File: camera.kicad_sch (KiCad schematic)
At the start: 12 parts, among them J2 FPC-05F-22PH20, Q1 BSS138PW,115, Q2 BSS138PW,115, U1 AM6254ATCGHAALW

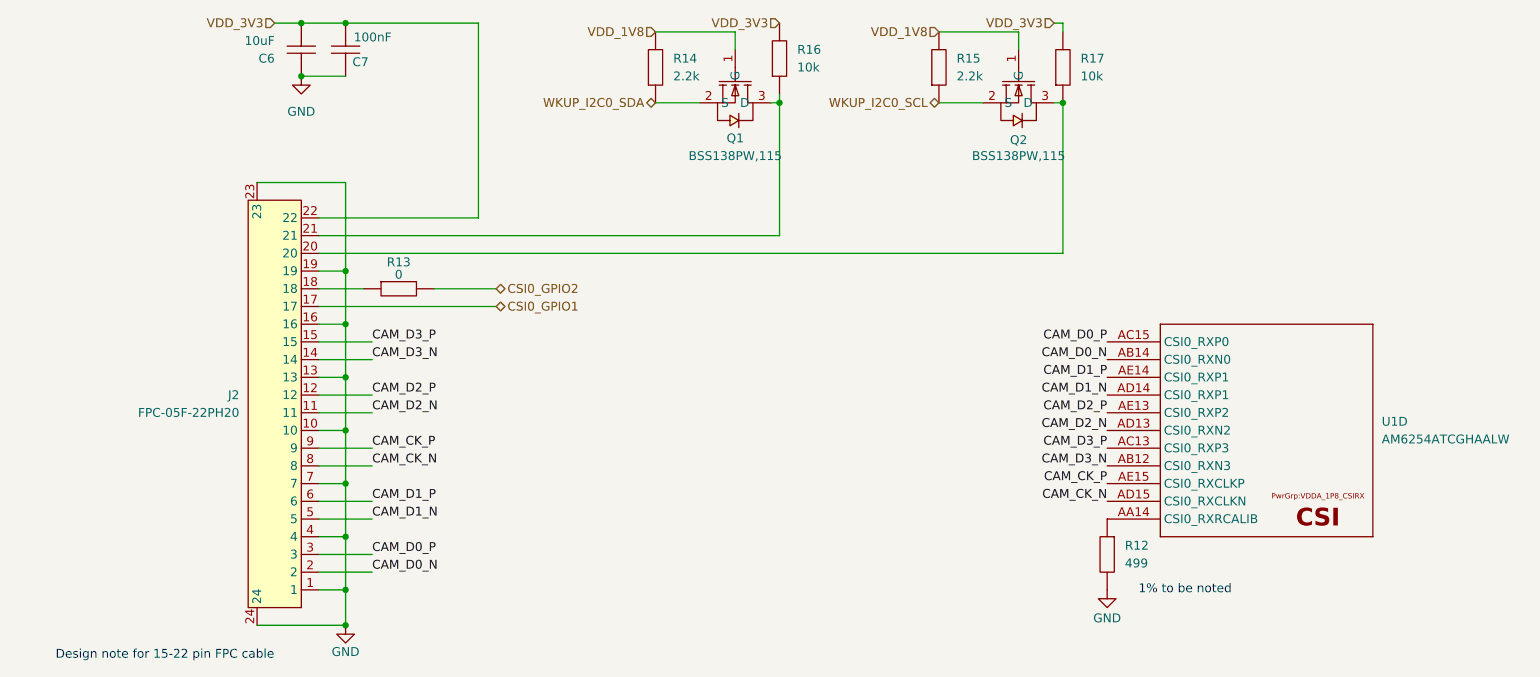
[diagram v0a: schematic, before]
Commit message: SD card changes
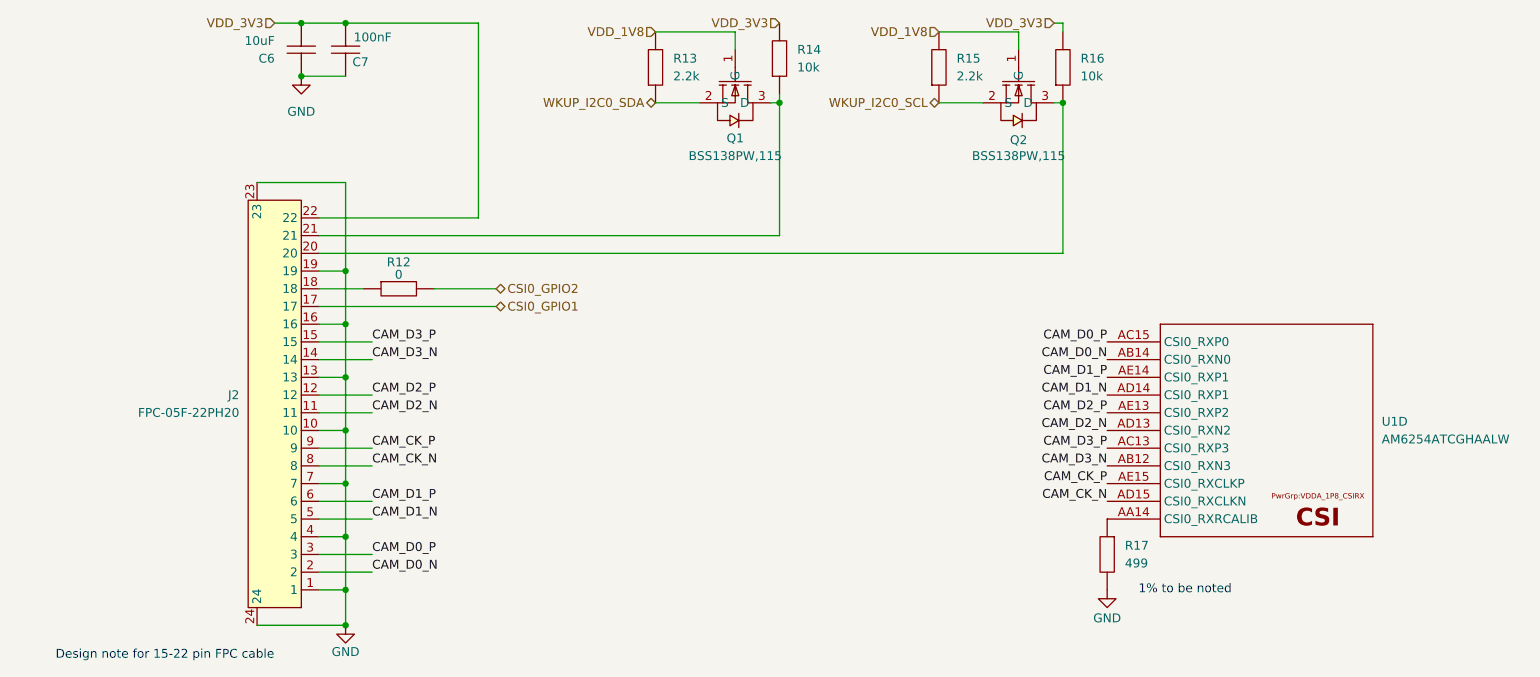
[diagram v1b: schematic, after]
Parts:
- renumbered R13 to R12, R14 to R13, R16 to R14, R17 to R16, R12 to R17
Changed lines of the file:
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@@
 		(dnp no)
 		(fields_autoplaced yes)
-		(property "Reference" "#PWR016"
+		(property "Reference" "#PWR014"
 			(at 62.23 38.1 0)
 			(effects
@@
 			(project ""
 				(path "/30d6913c-7aa4-4f56-9882-2ba08f7e2cce/0111536d-88df-4dfc-a217-9c0dd361d8c8"
-					(reference "#PWR016")
+					(reference "#PWR014")
 					(unit 1)
 				)
@@
 		(dnp no)
 		(fields_autoplaced yes)
-		(property "Reference" "R12"
+		(property "Reference" "R17"
 			(at 180.34 99.0599 90)
 			(effects
@@
 			(project ""
 				(path "/30d6913c-7aa4-4f56-9882-2ba08f7e2cce/0111536d-88df-4dfc-a217-9c0dd361d8c8"
-					(reference "R12")
+					(reference "R17")
 					(unit 1)
 				)
@@
 		(dnp no)
 		(fields_autoplaced yes)
-		(property "Reference" "R16"
+		(property "Reference" "R14"
 			(at 133.35 27.9399 90)
 			(effects
@@
 			(project ""
 				(path "/30d6913c-7aa4-4f56-9882-2ba08f7e2cce/0111536d-88df-4dfc-a217-9c0dd361d8c8"
-					(reference "R16")
+					(reference "R14")
 					(unit 1)
 				)
@@
 		(on_board yes)
 		(dnp no)
-		(property "Reference" "R13"
+		(property "Reference" "R12"
 			(at 76.2 58.42 0)
 			(effects
@@
 			(project ""
 				(path "/30d6913c-7aa4-4f56-9882-2ba08f7e2cce/0111536d-88df-4dfc-a217-9c0dd361d8c8"
-					(reference "R13")
+					(reference "R12")
 					(unit 1)
 				)
@@
 		(on_board yes)
 		(dnp no)
-		(property "Reference" "#PWR014"
+		(property "Reference" "#PWR015"
 			(at 68.58 116.84 0)
 			(effects
@@
 			(project ""
 				(path "/30d6913c-7aa4-4f56-9882-2ba08f7e2cce/0111536d-88df-4dfc-a217-9c0dd361d8c8"
-					(reference "#PWR014")
+					(reference "#PWR015")
 					(unit 1)
 				)
@@
 		(dnp no)
 		(fields_autoplaced yes)
-		(property "Reference" "R17"
+		(property "Reference" "R16"
 			(at 173.99 29.2099 90)
 			(effects
@@
 			(project "dashcam"
 				(path "/30d6913c-7aa4-4f56-9882-2ba08f7e2cce/0111536d-88df-4dfc-a217-9c0dd361d8c8"
-					(reference "R17")
+					(reference "R16")
 					(unit 1)
 				)
@@
 		(dnp no)
 		(fields_autoplaced yes)
-		(property "Reference" "R14"
+		(property "Reference" "R13"
 			(at 115.57 29.2099 90)
 			(effects
@@
 			(project ""
 				(path "/30d6913c-7aa4-4f56-9882-2ba08f7e2cce/0111536d-88df-4dfc-a217-9c0dd361d8c8"
-					(reference "R14")
+					(reference "R13")
 					(unit 1)
 				)
@@
 		(on_board yes)
 		(dnp no)
-		(property "Reference" "#PWR015"
+		(property "Reference" "#PWR016"
 			(at 177.8 111.76 0)
 			(effects
@@
 			(project ""
 				(path "/30d6913c-7aa4-4f56-9882-2ba08f7e2cce/0111536d-88df-4dfc-a217-9c0dd361d8c8"
-					(reference "#PWR015")
+					(reference "#PWR016")
 					(unit 1)
 				)
